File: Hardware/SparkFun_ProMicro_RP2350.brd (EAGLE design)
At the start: 17.8 x 33 mm, 114 parts, among them J2 QWIIC_RIGHT_ANGLE, J5 USB Female Type C Connector, U1 3.3V, U2 RP2350A, U3 WS2812-2020, U4 W25QXX128MBIT, Y1 12MHz

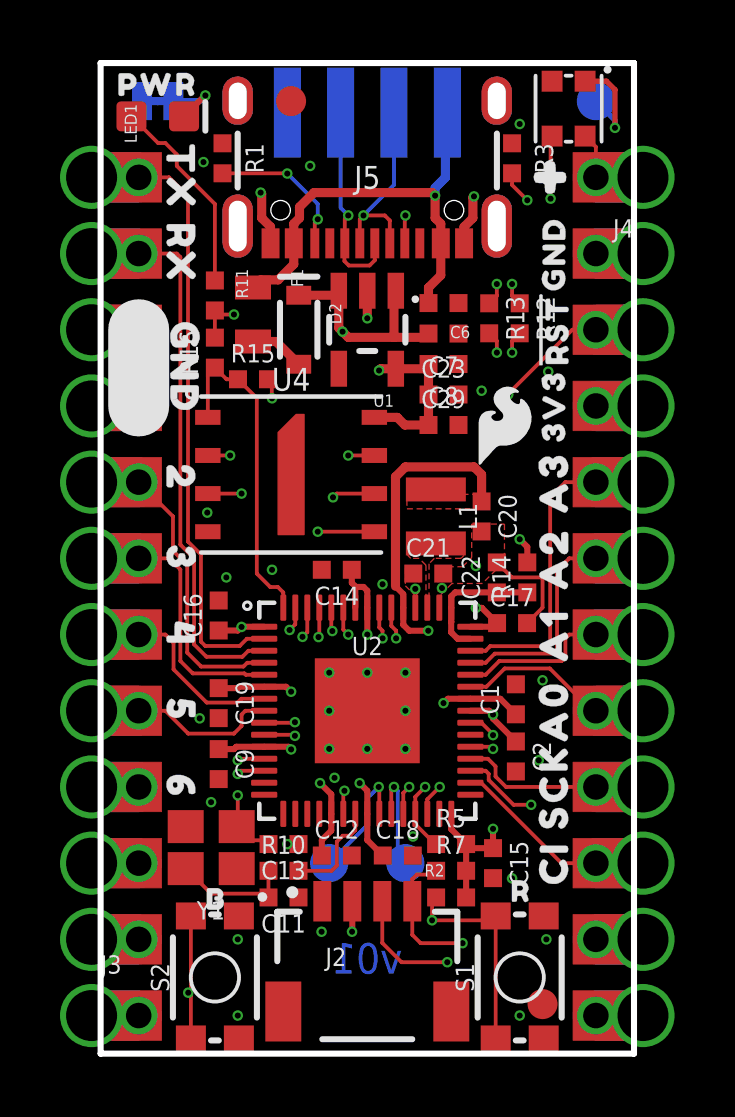
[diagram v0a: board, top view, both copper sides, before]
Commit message: More cleanup
Add test point for BOOT net
Nudge a few traces and vias to improve copper pours
Approve DRC errors
Fix traces overlapping vias
Fix acid traps
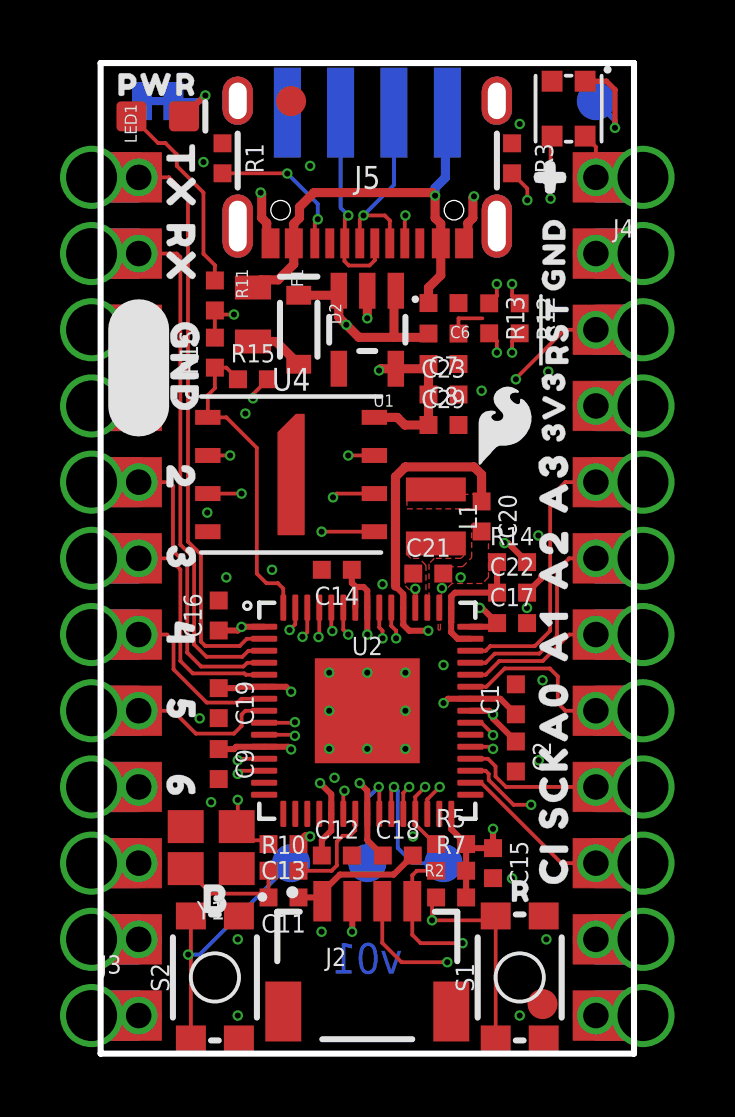
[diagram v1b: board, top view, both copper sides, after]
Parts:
- added TP4: TEST-POINT3X5, SparkFun-Connectors:PAD.03X.05
- added U$38: (no value), output:B0
- moved U$35 1.27 mm to (11.3, 4.95)
- moved TP1 1.27 mm to (8.89, 6.35)
- moved TP2 1.27 mm to (11.4, 6.35)
- moved U$18 1.27 mm to (8.76, 4.95)
- moved R14 0.72 mm to (13.7, 16.4), turned to 0 degrees
- moved C22 0.72 mm to (13.7, 15.4), turned to 0 degrees
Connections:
- net BOOT: now also TP4.1
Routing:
- net BOOT: track 25.8 -> 29.5 mm
- net GND: track 8.29 -> 11.7 mm, vias 35 -> 39
- net SWDIO: track 3.63 -> 4.75 mm
- net 2: track 10.7 -> 11.3 mm
- net SWDCK: track 4.13 -> 3.60 mm
- net A0: track 6.59 -> 7.11 mm

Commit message: Change C20 and C21 from 2.2uF to 10uF
Recommended by hardware guidelines
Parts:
- C20, C21: value 2.2uF -> 10uF
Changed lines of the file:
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@@
 <attribute name="VALUE" x="12.392" y="24.511" size="0.6096" layer="27" font="vector" ratio="20" rot="R270" align="top-center"/>
 </element>
-<element name="C20" library="SparkFun-Capacitors" package="0402-TIGHT" value="2.2uF" x="12.7" y="17.907" smashed="yes" rot="R270">
+<element name="C20" library="SparkFun-Capacitors" package="0402-TIGHT" value="10uF" x="12.7" y="17.907" smashed="yes" rot="R270">
 <attribute name="NAME" x="13.262" y="17.907" size="0.6096" layer="25" font="vector" ratio="20" rot="R270" align="bottom-center"/>
-<attribute name="PROD_ID" value="CAP-14232" x="-29.21" y="20.447" size="1.778" layer="27" font="vector" ratio="15" rot="R270" display="off"/>
-<attribute name="VALUE" x="12.138" y="17.907" size="0.6096" layer="27" font="vector" ratio="20" rot="R270" align="top-center"/>
+<attribute name="PROD_ID" value="CAP-14848" x="-29.21" y="20.447" size="1.778" layer="27" font="vector" ratio="15" rot="R270" display="off"/>
+<attribute name="VALUE" value="10uF" x="12.138" y="17.907" size="0.6096" layer="27" font="vector" ratio="20" rot="R270" align="top-center"/>
 </element>
-<element name="C21" library="SparkFun-Capacitors" package="0402-TIGHT" value="2.2uF" x="10.922" y="16.002" smashed="yes">
+<element name="C21" library="SparkFun-Capacitors" package="0402-TIGHT" value="10uF" x="10.922" y="16.002" smashed="yes">
 <attribute name="NAME" x="10.922" y="16.564" size="0.6096" layer="25" font="vector" ratio="20" align="bottom-center"/>
-<attribute name="PROD_ID" value="CAP-14232" x="4.572" y="-29.718" size="1.778" layer="27" font="vector" ratio="15" display="off"/>
-<attribute name="VALUE" x="10.922" y="15.44" size="0.6096" layer="27" font="vector" ratio="20" align="top-center"/>
+<attribute name="PROD_ID" value="CAP-14848" x="4.572" y="-29.718" size="1.778" layer="27" font="vector" ratio="15" display="off"/>
+<attribute name="VALUE" value="10uF" x="10.922" y="15.44" size="0.6096" layer="27" font="vector" ratio="20" align="top-center"/>
 </element>
 <element name="R14" library="SparkFun-Resistors" package="0402-TIGHT" value="10Ω" x="13.716" y="16.383" smashed="yes">

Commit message: Design review updates
Change regulator to RT9080
Add USB shield jumper and polygon to connect USB shield pads
Change PWR jumper silk to just be "P" and orient at 90 with silk polygon to connect it
Remove C6
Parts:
- removed C6: 1.0uF, SparkFun-Capacitors:0402-TIGHT
- removed U$41: (no value), output:#PWR#0
- added SHLD: JUMPER-SMT_2_NC_TRACE_SILK, SparkFun-Jumpers:SMT-JUMPER_2_NC_TRACE_SILK
- added U$43: (no value), output:#SHLD#0
- added U$44: (no value), output:B1
- U$36: device output:B0 -> output:#P#0
- U1: value 3.3V -> RT9080-33GJ5
- moved U$36 25.2 mm to (3.30, 30.4), flipped to the bottom
- moved U$3 16.2 mm to (5.71, 10.2), turned to 270 degrees
- moved C29 1.02 mm to (11.4, 22.0)
- moved C8 1.02 mm to (11.4, 24.0)
- moved C23 1.02 mm to (11.4, 23.0)
- moved C7 1.02 mm to (11.4, 25.0)
- renumbered JP3 to PWR
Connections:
- new net SHLD: J5.SHLD1, J5.SHLD2, J5.SHLD3, J5.SHLD4, SHLD.1
- net GND: now also SHLD.2; no longer C6.1
- net V_USB: no longer C6.2
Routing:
- net GND: track 11.7 -> 14.3 mm
- net SHLD: track 0.00 -> 2.50 mm
- net V_USB: track 15.2 -> 13.0 mm
- added copper zone on layer 2, net SHLD

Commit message: Clean up schematic
Rearrange sections to use whole frame
Update section titles
Move power LED and Qwiic connector to their own sections
Add text to jumpers indicating their functions
Change power LED to new version and update resistor
Swap VREG_AVDD and VREG_VIN pins on RP235 symbol to give more space for inductor in schematic
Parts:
- L1: value 4.7μH_SHIELDED_INDUCTOR -> 4.7μH
- R11: value 1k -> 4.7k
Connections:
- net N$1 renamed LED_OUT
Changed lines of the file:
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@@
 </autorouter>
 <elements>
-<element name="R11" library="SparkFun-Resistors" package="0402-TIGHT" value="1k" x="3.81" y="25.273" smashed="yes" rot="R270">
+<element name="R11" library="SparkFun-Resistors" package="0402-TIGHT" value="4.7k" x="3.81" y="25.273" smashed="yes" rot="R270">
 <attribute name="NAME" x="4.5085" y="26.162" size="0.4064" layer="25" rot="R270"/>
-<attribute name="PROD_ID" value="RES-14342" x="3.81" y="25.273" size="1.778" layer="27" rot="R270" display="off"/>
-<attribute name="VALUE" value="1k" x="3.683" y="23.9395" size="0.4064" layer="27" rot="R270"/>
+<attribute name="PROD_ID" value="RES-15343" x="3.81" y="25.273" size="1.778" layer="27" rot="R270" display="off"/>
+<attribute name="VALUE" value="4.7k" x="3.683" y="23.9395" size="0.4064" layer="27" rot="R270"/>
 </element>
 <element name="LED1" library="SparkFun-LED" package="LED-0603" value="Red" x="1.905" y="31.242" smashed="yes">
 <attribute name="NAME" x="1.2065" y="30.353" size="0.4064" layer="25" rot="R90"/>
-<attribute name="PROD_ID" value="DIO-00819" x="1.905" y="31.242" size="1.778" layer="27" display="off"/>
+<attribute name="PROD_ID" value="DIO-17976" x="1.905" y="31.242" size="1.778" layer="27" display="off"/>
 <attribute name="VALUE" value="Red" x="2.0955" y="32.766" size="0.4064" layer="27" rot="R90"/>
 </element>
@@
 <attribute name="VALUE" x="14.405" y="11.811" size="0.6096" layer="27" font="vector" ratio="20" rot="R90" align="top-center"/>
 </element>
-<element name="L1" library="SparkFun-Coils" package="1008(2520)" value="4.7μH_SHIELDED_INDUCTOR" x="11.176" y="17.907" smashed="yes" rot="R270">
+<element name="L1" library="SparkFun-Coils" package="1008(2520)" value="4.7μH" x="11.176" y="17.907" smashed="yes" rot="R270">
 <attribute name="NAME" x="11.938" y="17.907" size="0.6096" layer="25" font="vector" ratio="20" rot="R270" align="bottom-center"/>
 <attribute name="PROD_ID" value="NDUC-14880" x="11.176" y="17.907" size="1.778" layer="27" font="vector" ratio="15" rot="R270" display="off"/>
@@
 <signal name="RP_D+">
 <contactref element="R13" pad="1"/>
-<contactref element="JP14" pad="D+"/>
 <contactref element="J5" pad="A6"/>
 <contactref element="J5" pad="B6"/>
@@
 <wire x1="8.128" y1="26.416" x2="8.128" y2="26.998" width="0.127" layer="1"/>
 <wire x1="8.128" y1="26.998" x2="8.14" y2="27.01" width="0.127" layer="1"/>
+<wire x1="8.001" y1="28.194" x2="8.255" y2="27.94" width="0.127" layer="16"/>
+<contactref element="JP14" pad="D+"/>
 <wire x1="8.001" y1="31.369" x2="8.001" y2="28.194" width="0.127" layer="16"/>
-<wire x1="8.001" y1="28.194" x2="8.255" y2="27.94" width="0.127" layer="16"/>
 </signal>
 <signal name="RP_D-">
 <contactref element="R12" pad="1"/>
-<contactref element="JP14" pad="D-"/>
 <contactref element="J5" pad="A7"/>
 <contactref element="J5" pad="B7"/>
@@
 <wire x1="8.64" y1="27.01" x2="8.64" y2="27.817" width="0.127" layer="1"/>
 <wire x1="8.64" y1="27.817" x2="8.763" y2="27.94" width="0.127" layer="1"/>
+<wire x1="9.779" y1="28.956" x2="8.763" y2="27.94" width="0.127" layer="16"/>
+<contactref element="JP14" pad="D-"/>
 <wire x1="9.779" y1="31.369" x2="9.779" y2="28.956" width="0.127" layer="16"/>
-<wire x1="9.779" y1="28.956" x2="8.763" y2="27.94" width="0.127" layer="16"/>
 </signal>
 <signal name="BOOT">
@@
 <wire x1="13.081" y1="10.6172" x2="12.7" y2="10.9982" width="0.127" layer="2"/>
 </signal>
-<signal name="N$1">
-<contactref element="U3" pad="1"/>
+<signal name="LED_OUT">
 <contactref element="TP3" pad="1"/>
 <wire x1="16.51" y1="31.75" x2="17.145" y2="31.115" width="0.1778" layer="16"/>
@@
 <via x="17.145" y="30.861" extent="1-16" drill="0.2"/>
 <wire x1="17.145" y1="30.861" x2="17.145" y2="32.131" width="0.1778" layer="1"/>
-<wire x1="16.861" y1="32.415" x2="16.15" y2="32.415" width="0.1778" layer="1"/>
-<wire x1="17.145" y1="32.131" x2="16.861" y2="32.415" width="0.1778" layer="1"/>
+<wire x1="16.861" y1="32.415" x2="17.145" y2="32.131" width="0.1778" layer="1"/>
+<contactref element="U3" pad="1"/>
+<wire x1="16.15" y1="32.415" x2="16.861" y2="32.415" width="0.1778" layer="1"/>
 </signal>
 <signal name="VDDA">

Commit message: Update WS2812 symbol
Use new version so Eagle stops complaining
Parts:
- U3: value WS2812-2020 -> WS2812_2020
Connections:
- removed net LED_OUT: TP3.1, U3.1
- new net WS2812-DO: TP3.1, U3.DO
- net 25/WS2812-DI: now also U3.DI; no longer U3.3
- net GND: now also U3.GND; no longer U3.2
- net RAW: now also U3.VCC; no longer U3.4
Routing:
- net WS2812-DO: track 0.00 -> 3.53 mm, vias 0 -> 1
- net LED_OUT: track 3.53 -> 0.00 mm, vias 1 -> 0
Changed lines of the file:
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@@
 <element name="U$76" library="output" package="TX0" value="" x="2.667" y="29.21" smashed="yes" rot="R270"/>
 <element name="U$2" library="output" package="GND_0" value="" x="15.113" y="26.797" smashed="yes" rot="R90"/>
-<element name="U3" library="SparkFun-LED" package="WS2812-2020" value="WS2812-2020" x="15.6" y="31.5" smashed="yes" rot="R90">
+<element name="U3" library="SparkFun-LED" package="WS2812-2020" value="WS2812_2020" x="15.6" y="31.5" smashed="yes" rot="R90">
 <attribute name="PROD_ID" value="DIO-15591" x="15.6" y="31.5" size="1.778" layer="27" rot="R90" display="off"/>
 </element>
@@
 <via x="10.16" y="11.43" extent="1-16" drill="0.2"/>
 <via x="8.89" y="12.7" extent="1-16" drill="0.2"/>
-<contactref element="U3" pad="2"/>
 <contactref element="U2" pad="EPAD"/>
 <contactref element="U2" pad="47"/>
@@
 <wire x1="11.36325" y1="24.511" x2="11.32995" y2="24.4777" width="0.127" layer="1"/>
 <wire x1="11.32995" y1="24.4777" x2="10.414" y2="24.4777" width="0.127" layer="1"/>
+<contactref element="U3" pad="GND"/>
 </signal>
 <signal name="N$38">
@@
 <wire x1="16.1163" y1="29.6037" x2="16.51" y2="29.21" width="0.3048" layer="15"/>
 <wire x1="8.1865375" y1="29.6037" x2="16.1163" y2="29.6037" width="0.3048" layer="15"/>
-<contactref element="U3" pad="4"/>
-<wire x1="16.15" y1="30.585" x2="16.51" y2="30.225" width="0.127" layer="1"/>
 <wire x1="16.51" y1="30.225" x2="16.51" y2="29.21" width="0.127" layer="1"/>
 <wire x1="9.84" y1="25.4301" x2="10.5189" y2="25.4301" width="0.3048" layer="1"/>
 <wire x1="10.5189" y1="25.4301" x2="10.93" y2="25.019" width="0.3048" layer="1"/>
+<contactref element="U3" pad="VCC"/>
+<wire x1="16.15" y1="30.585" x2="16.51" y2="30.225" width="0.127" layer="1"/>
 </signal>
 <signal name="A3">
@@
 </signal>
 <signal name="25/WS2812-DI">
-<contactref element="U3" pad="3"/>
 <via x="15" y="28.5" extent="1-16" drill="0.2"/>
 <wire x1="14.1843" y1="22.6043" x2="14.1843" y2="15.4543" width="0.127" layer="2"/>
 <wire x1="15" y1="23.42" x2="14.1843" y2="22.6043" width="0.127" layer="2"/>
 <wire x1="15" y1="23.42" x2="15" y2="28.5" width="0.127" layer="2"/>
-<wire x1="15" y1="28.5" x2="15" y2="30.535" width="0.127" layer="1"/>
-<wire x1="15" y1="30.535" x2="15.05" y2="30.585" width="0.127" layer="1"/>
+<wire x1="15" y1="30.535" x2="15" y2="28.5" width="0.127" layer="1"/>
 <contactref element="U2" pad="37"/>
 <wire x1="12.3265" y1="11.03" x2="12.6936" y2="11.03" width="0.127" layer="1"/>
@@
 <wire x1="12.7" y1="13.97" x2="12.7" y2="10.9982" width="0.127" layer="2"/>
 <wire x1="13.081" y1="10.6172" x2="12.7" y2="10.9982" width="0.127" layer="2"/>
-</signal>
-<signal name="LED_OUT">
+<contactref element="U3" pad="DI"/>
+<wire x1="15.05" y1="30.585" x2="15" y2="30.535" width="0.127" layer="1"/>
+</signal>
+<signal name="WS2812-DO">
 <contactref element="TP3" pad="1"/>
 <wire x1="16.51" y1="31.75" x2="17.145" y2="31.115" width="0.1778" layer="16"/>
@@
 <wire x1="17.145" y1="30.861" x2="17.145" y2="32.131" width="0.1778" layer="1"/>
 <wire x1="16.861" y1="32.415" x2="17.145" y2="32.131" width="0.1778" layer="1"/>
-<contactref element="U3" pad="1"/>
+<contactref element="U3" pad="DO"/>
 <wire x1="16.15" y1="32.415" x2="16.861" y2="32.415" width="0.1778" layer="1"/>
 </signal>

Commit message: Use castellated pad device from SparkFun lib
Remove dependency of "Castellated" lib
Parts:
- J3, J4: device Castellated:1X12_CASTELLATED -> SparkFun-Connectors:1X12_CASTELLATED
